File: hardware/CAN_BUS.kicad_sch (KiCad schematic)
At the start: 15 parts, among them U7 ADM3057ExRW

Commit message: reorganization of project folders acording to templates
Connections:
- net +3.3V renamed +3V3

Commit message: added missing files
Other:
- moved on the sheet: C34, C39, C40, C41, C66, FB3, FB5, R15, U7

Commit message: initial component placement
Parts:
- C66: footprint Samacsys:CAPC5728X280N -> XiaoS3:CAPC5727X254N; Mouser Part Number 791-S252B222K502CT -> 77-HV2225Y472KXVATHV
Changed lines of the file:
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@@
 			)
 		)
-		(property "Footprint" "Samacsys:CAPC5728X280N"
+		(property "Footprint" "XiaoS3:CAPC5727X254N"
 			(at 186.36 120.65 0)
 			(hide yes)
@@
 			)
 		)
-		(property "Datasheet" ""
+		(property "Datasheet" "https://www.vishay.com/docs/45228/hvseries.pdf"
 			(at 286.36 120.65 0)
 			(hide yes)
@@
 			)
 		)
-		(property "Mouser Part Number" "791-S252B222K502CT"
+		(property "Mouser Part Number" "77-HV2225Y472KXVATHV"
 			(at 586.36 120.65 0)
 			(hide yes)

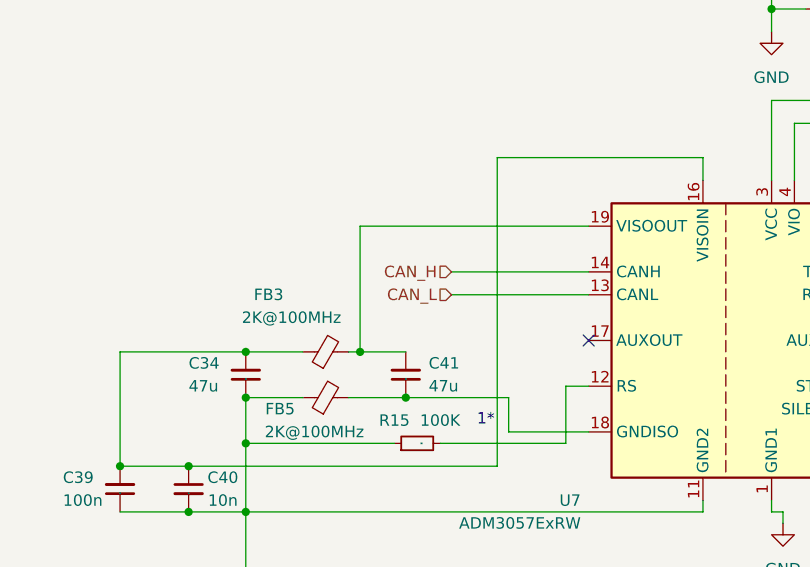
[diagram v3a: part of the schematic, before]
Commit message: changed layout
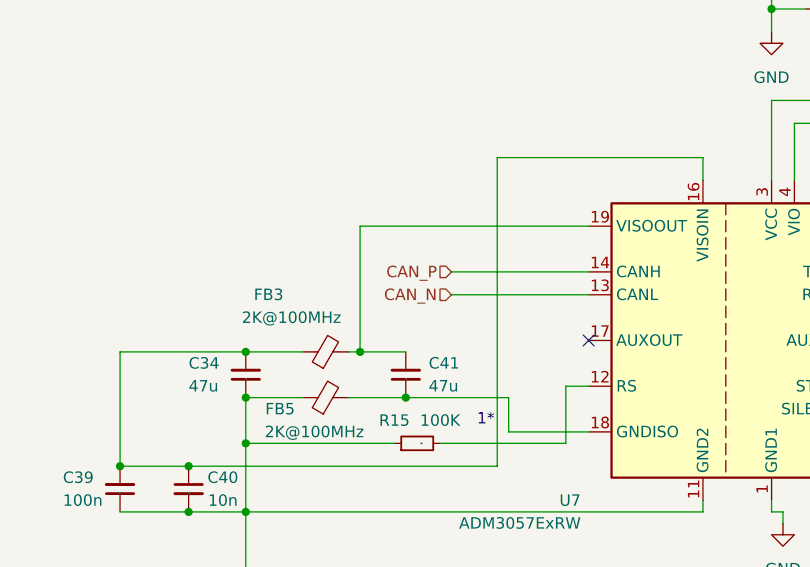
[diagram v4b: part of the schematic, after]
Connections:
- net CAN_H renamed CAN_P
- net CAN_L renamed CAN_N
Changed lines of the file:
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@@
 		)
 	)
-	(hierarchical_label "CAN_H"
+	(hierarchical_label "CAN_P"
 		(shape input)
 		(at 113.03 88.9 180)
@@
 		)
 	)
-	(hierarchical_label "CAN_L"
+	(hierarchical_label "CAN_N"
 		(shape input)
 		(at 113.03 91.44 180)
